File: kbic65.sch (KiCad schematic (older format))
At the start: 150 parts, among them U1 ProMicro

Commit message: Changed diode to row2col instead to make better wiring, rearranging diode footprints
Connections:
- net COL0: now also D_1.1 (K), D_A1.1 (K), D_CpsLck1.1 (K), D_Esc1.1 (K), D_ISO_BKSLSH1.1 (K), D_LCtrl1.1 (K), D_LShift1.1 (K), D_Q1.1 (K), D_Tab1.1 (K); no longer MX_1.1 (COL), MX_A1.1 (COL), MX_CpsLck1.1 (COL), MX_CpsLck2_Stepped1.1 (COL), MX_Esc1.1 (COL), MX_ISO_BKSLSH1.1 (COL), MX_LCtrl1.1 (COL), MX_LShift_ANSI1.1 (COL), MX_LShift_ISO1.1 (COL), MX_Q1.1 (COL), MX_Tab1.1 (COL)
- net COL1: now also D_2.1 (K), D_3.1 (K), D_D1.1 (K), D_E1.1 (K), D_LWin1.1 (K), D_S1.1 (K), D_W1.1 (K), D_X1.1 (K), D_Z1.1 (K); no longer MX_2.1 (COL), MX_3.1 (COL), MX_D1.1 (COL), MX_E1.1 (COL), MX_LWin1.1 (COL), MX_S1.1 (COL), MX_W1.1 (COL), MX_X1.1 (COL), MX_Z1.1 (COL)
- net COL2: now also D_4.1 (K), D_5.1 (K), D_C1.1 (K), D_F1.1 (K), D_G1.1 (K), D_LAlt1.1 (K), D_R1.1 (K), D_T1.1 (K), D_V1.1 (K); no longer MX_4.1 (COL), MX_5.1 (COL), MX_C1.1 (COL), MX_F1.1 (COL), MX_G1.1 (COL), MX_LAlt1.1 (COL), MX_R1.1 (COL), MX_T1.1 (COL), MX_V1.1 (COL)
- net COL3: now also D_6.1 (K), D_7.1 (K), D_B1.1 (K), D_H1.1 (K), D_J1.1 (K), D_N1.1 (K), D_Space1.1 (K), D_U1.1 (K), D_Y1.1 (K); no longer MX_6.1 (COL), MX_7.1 (COL), MX_B1.1 (COL), MX_H1.1 (COL), MX_J1.1 (COL), MX_N1.1 (COL), MX_Space1_6.25u1.1 (COL), MX_Space2_6u1.1 (COL), MX_U1.1 (COL), MX_Y1.1 (COL)
- net COL4: now also D_8.1 (K), D_9.1 (K), D_Comma1.1 (K), D_I1.1 (K), D_K1.1 (K), D_L1.1 (K), D_M1.1 (K), D_O1.1 (K), D_RAlt1.1 (K); no longer MX_8.1 (COL), MX_9.1 (COL), MX_Comma1.1 (COL), MX_I1.1 (COL), MX_K1.1 (COL), MX_L1.1 (COL), MX_M1.1 (COL), MX_O1.1 (COL)
- net COL5: now also D_0.1 (K), D_@1.1 (K), D_Dot1.1 (K), D_FwdSlsh1.1 (K), D_Hyphen1.1 (K), D_LBKT1.1 (K), D_P1.1 (K), D_RWin1.1 (K), D_SemiCol1.1 (K); no longer MX_0.1 (COL), MX_@1.1 (COL), MX_Dot1.1 (COL), MX_FwdSlsh1.1 (COL), MX_Hyphen1.1 (COL), MX_LBKT1.1 (COL), MX_P1.1 (COL), MX_RWin1.1 (COL), MX_RWin2_1.25u_RCtrl1.1 (COL), MX_SemiCol1.1 (COL)
- net COL6: now also D_BKSLSH1.1 (K), D_BkSp1.1 (K), D_Enter1.1 (K), D_Equal1.1 (K), D_RBKT1.1 (K), D_RCtrl1.1 (K), D_RShift1.1 (K), D_Up1.1 (K); no longer MX_BkSlash2_ISO_Enter1.1 (COL), MX_BkSlsh1.1 (COL), MX_BkSp1.1 (COL), MX_BkSp3_2u1.1 (COL), MX_Enter1.1 (COL), MX_Enter2_ISO_Hash1.1 (COL), MX_Equal1.1 (COL), MX_RBKT1.1 (COL), MX_RCtrl1.1 (COL), MX_RShift1.1 (COL), MX_Up1.1 (COL)
- net COL7: now also D_BkSp2.1 (K), D_Del1.1 (K), D_Down1.1 (K), D_Left1.1 (K), D_PgDn1.1 (K), D_PgUp1.1 (K), D_Right1.1 (K), D_Tilde1.1 (K); no longer MX_BkSp2.1 (COL), MX_Del1.1 (COL), MX_Down1.1 (COL), MX_Left1.1 (COL), MX_PgDn1.1 (COL), MX_PgUp1.1 (COL), MX_Right1.1 (COL), MX_Tilde1.1 (COL)
- net ROW0: now also MX_1.2 (ROW), MX_3.2 (ROW), MX_5.2 (ROW), MX_7.2 (ROW), MX_9.2 (ROW), MX_BkSp1.2 (ROW), MX_BkSp3_2u1.2 (ROW), MX_Hyphen1.2 (ROW), MX_Tilde1.2 (ROW); no longer D_1.1 (K), D_3.1 (K), D_5.1 (K), D_7.1 (K), D_9.1 (K), D_BkSp1.1 (K), D_Hyphen1.1 (K), D_Tilde1.1 (K)
- net ROW1: now also MX_0.2 (ROW), MX_2.2 (ROW), MX_4.2 (ROW), MX_6.2 (ROW), MX_8.2 (ROW), MX_BkSp2.2 (ROW), MX_Equal1.2 (ROW), MX_Esc1.2 (ROW); no longer D_0.1 (K), D_2.1 (K), D_4.1 (K), D_6.1 (K), D_8.1 (K), D_BkSp2.1 (K), D_Equal1.1 (K), D_Esc1.1 (K)
- net ROW2: now also MX_BkSlash2_ISO_Enter1.2 (ROW), MX_BkSlsh1.2 (ROW), MX_E1.2 (ROW), MX_LBKT1.2 (ROW), MX_O1.2 (ROW), MX_Q1.2 (ROW), MX_T1.2 (ROW), MX_U1.2 (ROW); no longer D_BKSLSH1.1 (K), D_E1.1 (K), D_LBKT1.1 (K), D_O1.1 (K), D_Q1.1 (K), D_T1.1 (K), D_U1.1 (K)
- net ROW3: now also MX_Del1.2 (ROW), MX_I1.2 (ROW), MX_P1.2 (ROW), MX_R1.2 (ROW), MX_RBKT1.2 (ROW), MX_Tab1.2 (ROW), MX_W1.2 (ROW), MX_Y1.2 (ROW); no longer D_Del1.1 (K), D_I1.1 (K), D_P1.1 (K), D_R1.1 (K), D_RBKT1.1 (K), D_Tab1.1 (K), D_W1.1 (K), D_Y1.1 (K)
- net ROW4: now also MX_@1.2 (ROW), MX_A1.2 (ROW), MX_D1.2 (ROW), MX_G1.2 (ROW), MX_J1.2 (ROW), MX_L1.2 (ROW), MX_PgUp1.2 (ROW); no longer D_@1.1 (K), D_A1.1 (K), D_D1.1 (K), D_G1.1 (K), D_J1.1 (K), D_L1.1 (K), D_PgUp1.1 (K)
- net ROW5: now also MX_CpsLck1.2 (ROW), MX_CpsLck2_Stepped1.2 (ROW), MX_Enter1.2 (ROW), MX_Enter2_ISO_Hash1.2 (ROW), MX_F1.2 (ROW), MX_H1.2 (ROW), MX_K1.2 (ROW), MX_PgDn1.2 (ROW), MX_S1.2 (ROW), MX_SemiCol1.2 (ROW); no longer D_CpsLck1.1 (K), D_Enter1.1 (K), D_F1.1 (K), D_H1.1 (K), D_K1.1 (K), D_PgDn1.1 (K), D_S1.1 (K), D_SemiCol1.1 (K)
- net ROW6: now also MX_Comma1.2 (ROW), MX_FwdSlsh1.2 (ROW), MX_ISO_BKSLSH1.2 (ROW), MX_N1.2 (ROW), MX_Right1.2 (ROW), MX_Up1.2 (ROW), MX_V1.2 (ROW), MX_X1.2 (ROW); no longer D_Comma1.1 (K), D_FwdSlsh1.1 (K), D_ISO_BKSLSH1.1 (K), D_N1.1 (K), D_Right1.1 (K), D_Up1.1 (K), D_V1.1 (K), D_X1.1 (K)
- net ROW7: now also MX_B1.2 (ROW), MX_C1.2 (ROW), MX_Dot1.2 (ROW), MX_Down1.2 (ROW), MX_LShift_ANSI1.2 (ROW), MX_LShift_ISO1.2 (ROW), MX_M1.2 (ROW), MX_RShift1.2 (ROW), MX_Z1.2 (ROW); no longer D_B1.1 (K), D_C1.1 (K), D_Dot1.1 (K), D_Down1.1 (K), D_LShift1.1 (K), D_M1.1 (K), D_RShift1.1 (K), D_Z1.1 (K)
- net ROW8: now also MX_LAlt1.2 (ROW), MX_LCtrl1.2 (ROW), MX_LWin1.2 (ROW), MX_Left1.2 (ROW), MX_RAlt1_1u1.2 (ROW), MX_RAlt2_1.25u_6u_space1.2 (ROW), MX_RAlt3_1.25u_6.25u_space1.2 (ROW), MX_RCtrl1.2 (ROW), MX_RWin1.2 (ROW), MX_RWin2_1.25u_RCtrl1.2 (ROW), MX_Space1_6.25u1.2 (ROW), MX_Space2_6u1.2 (ROW); no longer D_LAlt1.1 (K), D_LCtrl1.1 (K), D_LWin1.1 (K), D_Left1.1 (K), D_RAlt1.1 (K), D_RCtrl1.1 (K), D_RWin1.1 (K), D_Space1.1 (K)
- net at D_1.2 (A): now also MX_1.1 (COL); no longer MX_1.2 (ROW)
- net at D_Esc1.2 (A): now also MX_Esc1.1 (COL); no longer MX_Esc1.2 (ROW)
- net at D_Q1.2 (A): now also MX_Q1.1 (COL); no longer MX_Q1.2 (ROW)
- net at D_Tab1.2 (A): now also MX_Tab1.1 (COL); no longer MX_Tab1.2 (ROW)
- net at D_3.2 (A): now also MX_3.1 (COL); no longer MX_3.2 (ROW)
- net at D_2.2 (A): now also MX_2.1 (COL); no longer MX_2.2 (ROW)
- net at D_E1.2 (A): now also MX_E1.1 (COL); no longer MX_E1.2 (ROW)
- net at D_W1.2 (A): now also MX_W1.1 (COL); no longer MX_W1.2 (ROW)
- net at D_5.2 (A): now also MX_5.1 (COL); no longer MX_5.2 (ROW)
- net at D_4.2 (A): now also MX_4.1 (COL); no longer MX_4.2 (ROW)
- net at D_T1.2 (A): now also MX_T1.1 (COL); no longer MX_T1.2 (ROW)
- net at D_R1.2 (A): now also MX_R1.1 (COL); no longer MX_R1.2 (ROW)
- net at D_7.2 (A): now also MX_7.1 (COL); no longer MX_7.2 (ROW)
- net at D_6.2 (A): now also MX_6.1 (COL); no longer MX_6.2 (ROW)
- net at D_U1.2 (A): now also MX_U1.1 (COL); no longer MX_U1.2 (ROW)
- net at D_Y1.2 (A): now also MX_Y1.1 (COL); no longer MX_Y1.2 (ROW)
- net at D_9.2 (A): now also MX_9.1 (COL); no longer MX_9.2 (ROW)
- net at D_8.2 (A): now also MX_8.1 (COL); no longer MX_8.2 (ROW)
- net at D_O1.2 (A): now also MX_O1.1 (COL); no longer MX_O1.2 (ROW)
- net at D_I1.2 (A): now also MX_I1.1 (COL); no longer MX_I1.2 (ROW)
- net at D_Hyphen1.2 (A): now also MX_Hyphen1.1 (COL); no longer MX_Hyphen1.2 (ROW)
- net at D_0.2 (A): now also MX_0.1 (COL); no longer MX_0.2 (ROW)
- net at D_LBKT1.2 (A): now also MX_LBKT1.1 (COL); no longer MX_LBKT1.2 (ROW)
- net at D_P1.2 (A): now also MX_P1.1 (COL); no longer MX_P1.2 (ROW)
- net at D_Equal1.2 (A): now also MX_Equal1.1 (COL); no longer MX_Equal1.2 (ROW)
- net at D_RBKT1.2 (A): now also MX_RBKT1.1 (COL); no longer MX_RBKT1.2 (ROW)
- net at D_Tilde1.2 (A): now also MX_Tilde1.1 (COL); no longer MX_Tilde1.2 (ROW)
- net at D_BkSp2.2 (A): now also MX_BkSp2.1 (COL); no longer MX_BkSp2.2 (ROW)
- net at D_Del1.2 (A): now also MX_Del1.1 (COL); no longer MX_Del1.2 (ROW)
- net at MX_RAlt1_1u1.1 (COL), MX_RAlt2_1.25u_6u_space1.1 (COL), MX_RAlt3_1.25u_6.25u_space1.1 (COL): now also D_RAlt1.2 (A)
- net at D_A1.2 (A): now also MX_A1.1 (COL); no longer MX_A1.2 (ROW)
- net at D_ISO_BKSLSH1.2 (A): now also MX_ISO_BKSLSH1.1 (COL); no longer MX_ISO_BKSLSH1.2 (ROW)
- net at D_D1.2 (A): now also MX_D1.1 (COL); no longer MX_D1.2 (ROW)
- net at D_S1.2 (A): now also MX_S1.1 (COL); no longer MX_S1.2 (ROW)
- net at D_X1.2 (A): now also MX_X1.1 (COL); no longer MX_X1.2 (ROW)
- net at D_Z1.2 (A): now also MX_Z1.1 (COL); no longer MX_Z1.2 (ROW)
- net at D_G1.2 (A): now also MX_G1.1 (COL); no longer MX_G1.2 (ROW)
- net at D_F1.2 (A): now also MX_F1.1 (COL); no longer MX_F1.2 (ROW)
- net at D_V1.2 (A): now also MX_V1.1 (COL); no longer MX_V1.2 (ROW)
- net at D_C1.2 (A): now also MX_C1.1 (COL); no longer MX_C1.2 (ROW)
- net at D_J1.2 (A): now also MX_J1.1 (COL); no longer MX_J1.2 (ROW)
- net at D_H1.2 (A): now also MX_H1.1 (COL); no longer MX_H1.2 (ROW)
- net at D_N1.2 (A): now also MX_N1.1 (COL); no longer MX_N1.2 (ROW)
- net at D_B1.2 (A): now also MX_B1.1 (COL); no longer MX_B1.2 (ROW)
- net at D_L1.2 (A): now also MX_L1.1 (COL); no longer MX_L1.2 (ROW)
- net at D_K1.2 (A): now also MX_K1.1 (COL); no longer MX_K1.2 (ROW)
- net at D_Comma1.2 (A): now also MX_Comma1.1 (COL); no longer MX_Comma1.2 (ROW)
- net at D_M1.2 (A): now also MX_M1.1 (COL); no longer MX_M1.2 (ROW)
- net at D_@1.2 (A): now also MX_@1.1 (COL); no longer MX_@1.2 (ROW)
- net at D_SemiCol1.2 (A): now also MX_SemiCol1.1 (COL); no longer MX_SemiCol1.2 (ROW)
- net at D_FwdSlsh1.2 (A): now also MX_FwdSlsh1.1 (COL); no longer MX_FwdSlsh1.2 (ROW)
- net at D_Dot1.2 (A): now also MX_Dot1.1 (COL); no longer MX_Dot1.2 (ROW)
- net at D_Up1.2 (A): now also MX_Up1.1 (COL); no longer MX_Up1.2 (ROW)
- net at D_RShift1.2 (A): now also MX_RShift1.1 (COL); no longer MX_RShift1.2 (ROW)
- net at D_PgUp1.2 (A): now also MX_PgUp1.1 (COL); no longer MX_PgUp1.2 (ROW)
- net at D_PgDn1.2 (A): now also MX_PgDn1.1 (COL); no longer MX_PgDn1.2 (ROW)
- net at D_Right1.2 (A): now also MX_Right1.1 (COL); no longer MX_Right1.2 (ROW)
- net at D_Down1.2 (A): now also MX_Down1.1 (COL); no longer MX_Down1.2 (ROW)
- net at D_LCtrl1.2 (A): now also MX_LCtrl1.1 (COL); no longer MX_LCtrl1.2 (ROW)
- net at D_LWin1.2 (A): now also MX_LWin1.1 (COL); no longer MX_LWin1.2 (ROW)
- net at D_LAlt1.2 (A): now also MX_LAlt1.1 (COL); no longer MX_LAlt1.2 (ROW)
- net at D_RCtrl1.2 (A): now also MX_RCtrl1.1 (COL); no longer MX_RCtrl1.2 (ROW)
- net at D_Left1.2 (A): now also MX_Left1.1 (COL); no longer MX_Left1.2 (ROW)
- new net: D_BkSp1.2 (A), MX_BkSp1.1 (COL), MX_BkSp3_2u1.1 (COL)
- new net: D_BKSLSH1.2 (A), MX_BkSlash2_ISO_Enter1.1 (COL), MX_BkSlsh1.1 (COL)
- new net: D_LShift1.2 (A), MX_LShift_ANSI1.1 (COL), MX_LShift_ISO1.1 (COL)
- new net: D_CpsLck1.2 (A), MX_CpsLck1.1 (COL), MX_CpsLck2_Stepped1.1 (COL)
- new net: D_Space1.2 (A), MX_Space1_6.25u1.1 (COL), MX_Space2_6u1.1 (COL)
- new net: D_RWin1.2 (A), MX_RWin1.1 (COL), MX_RWin2_1.25u_RCtrl1.1 (COL)
- new net: D_Enter1.2 (A), MX_Enter1.1 (COL), MX_Enter2_ISO_Hash1.1 (COL)
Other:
- moved on the sheet: D_0, D_1, D_2, D_3, D_4, D_5, D_6, D_7, D_8, D_9, D_@1, D_A1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

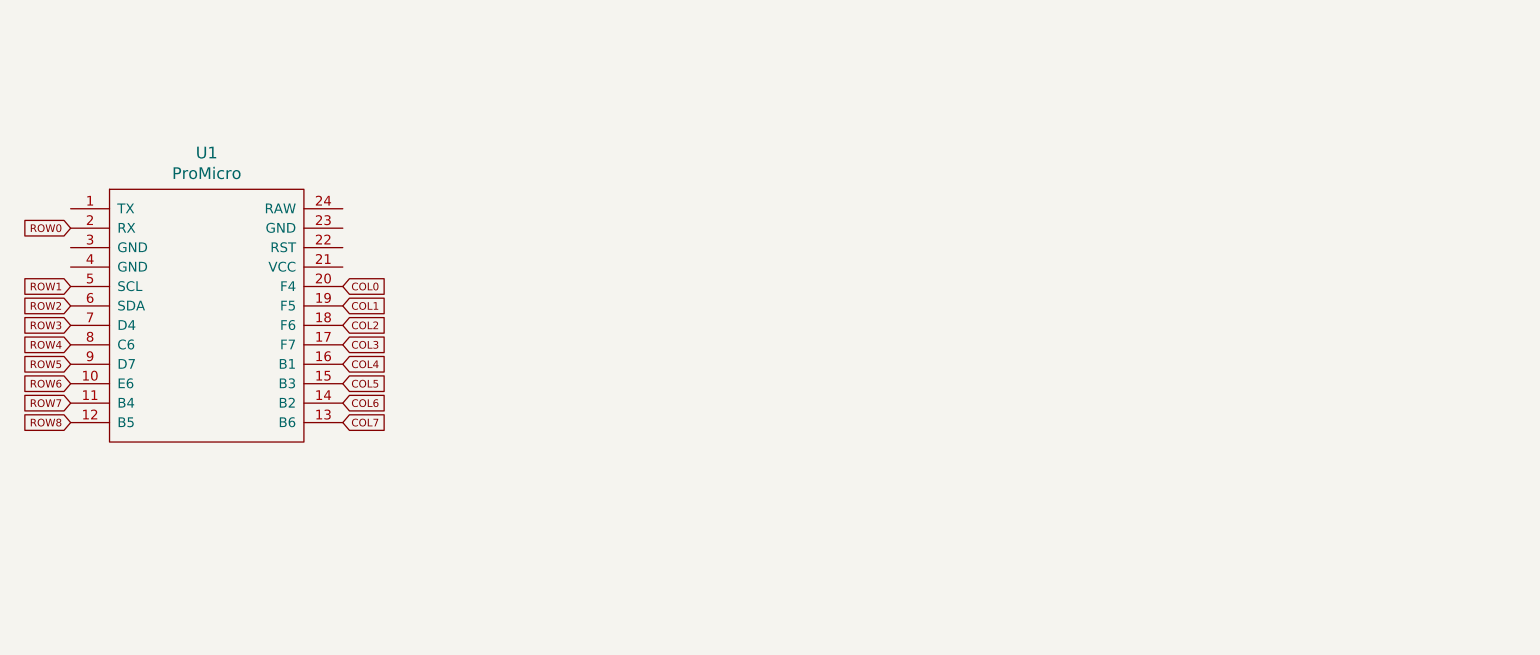
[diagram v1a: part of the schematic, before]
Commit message: Rearranged rows on promicro footprint
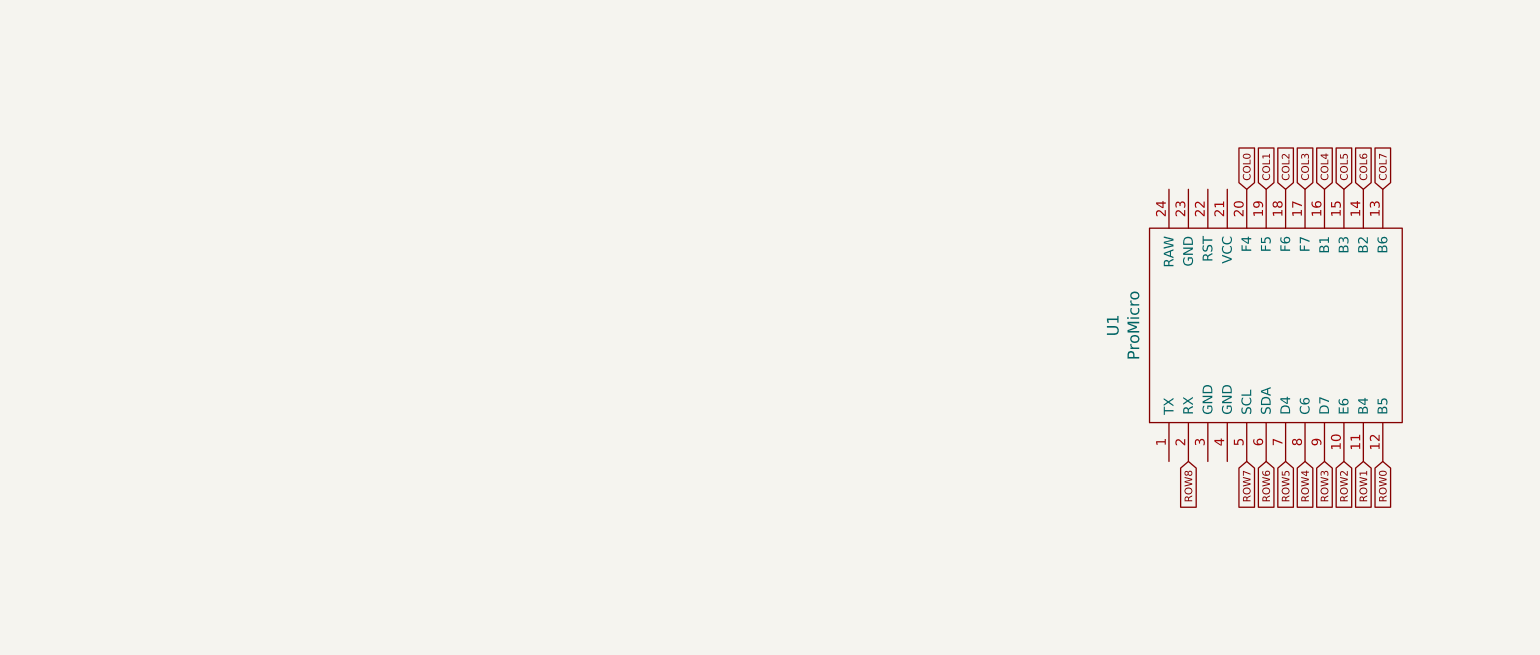
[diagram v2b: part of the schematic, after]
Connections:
- net ROW0: now also U1.12 (B5); no longer U1.2 (RX)
- net ROW1: now also U1.11 (B4); no longer U1.5 (SCL)
- net ROW2: now also U1.10 (E6); no longer U1.6 (SDA)
- net ROW3: now also U1.9 (D7); no longer U1.7 (D4)
- net ROW5: now also U1.7 (D4); no longer U1.9 (D7)
- net ROW6: now also U1.6 (SDA); no longer U1.10 (E6)
- net ROW7: now also U1.5 (SCL); no longer U1.11 (B4)
- net ROW8: now also U1.2 (RX); no longer U1.12 (B5)
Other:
- moved on the sheet: U1
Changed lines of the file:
@@
 	0    -1   -1   0
 $EndComp
-Text GLabel 3150 3350 0    39   Input ~ 0
+Text GLabel 8900 4550 3    39   Input ~ 0
+ROW8
+Text GLabel 9200 4550 3    39   Input ~ 0
+ROW7
+Text GLabel 9300 4550 3    39   Input ~ 0
+ROW6
+Text GLabel 9400 4550 3    39   Input ~ 0
+ROW5
+Text GLabel 9500 4550 3    39   Input ~ 0
+ROW4
+Text GLabel 9600 4550 3    39   Input ~ 0
+ROW3
+Text GLabel 9700 4550 3    39   Input ~ 0
+ROW2
+Text GLabel 9800 4550 3    39   Input ~ 0
+ROW1
+Text GLabel 9900 4550 3    39   Input ~ 0
 ROW0
-Text GLabel 3150 3650 0    39   Input ~ 0
-ROW1
-Text GLabel 3150 3750 0    39   Input ~ 0
-ROW2
-Text GLabel 3150 3850 0    39   Input ~ 0
-ROW3
-Text GLabel 3150 3950 0    39   Input ~ 0
-ROW4
-Text GLabel 3150 4050 0    39   Input ~ 0
-ROW5
-Text GLabel 3150 4150 0    39   Input ~ 0
-ROW6
-Text GLabel 3150 4250 0    39   Input ~ 0
-ROW7
-Text GLabel 3150 4350 0    39   Input ~ 0
-ROW8
-Text GLabel 4550 3650 2    39   Input ~ 0
+Text GLabel 9200 3150 1    39   Input ~ 0
 COL0
-Text GLabel 4550 3750 2    39   Input ~ 0
+Text GLabel 9300 3150 1    39   Input ~ 0
 COL1
-Text GLabel 4550 3850 2    39   Input ~ 0
+Text GLabel 9400 3150 1    39   Input ~ 0
 COL2
-Text GLabel 4550 3950 2    39   Input ~ 0
+Text GLabel 9500 3150 1    39   Input ~ 0
 COL3
-Text GLabel 4550 4050 2    39   Input ~ 0
+Text GLabel 9600 3150 1    39   Input ~ 0
 COL4
-Text GLabel 4550 4150 2    39   Input ~ 0
+Text GLabel 9700 3150 1    39   Input ~ 0
 COL5
-Text GLabel 4550 4250 2    39   Input ~ 0
+Text GLabel 9800 3150 1    39   Input ~ 0
 COL6
-Text GLabel 4550 4350 2    39   Input ~ 0
+Text GLabel 9900 3150 1    39   Input ~ 0
 COL7
 $Comp
 L promicro:ProMicro U1
 U 1 1 601A4F40
-P 3850 4000
-F 0 "U1" H 3850 5037 60  0000 C CNN
-F 1 "ProMicro" H 3850 4931 60  0000 C CNN
-F 2 "Keebio-Parts:ArduinoProMicro-ZigZag" H 3950 2950 60  0001 C CNN
-F 3 "" H 3950 2950 60  0000 C CNN
-	1    3850 4000
-	1    0    0    -1
+P 9550 3850
+F 0 "U1" H 9550 4887 60  0000 C CNN
+F 1 "ProMicro" H 9550 4781 60  0000 C CNN
+F 2 "Keebio-Parts:ArduinoProMicro-ZigZag" H 9650 2800 60  0001 C CNN
+F 3 "" H 9650 2800 60  0000 C CNN
+	1    9550 3850
+	0    -1   -1   0
 $EndComp
 $Comp
